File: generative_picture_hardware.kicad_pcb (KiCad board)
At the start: 2 copper layers, 100 x 100 mm, 73 parts, among them J1 e_Paper_HAT, J2 Conn_ARM_JTAG_SWD_10, J3 USB_C_Receptacle_USB2.0, Q1 PMN48XP, Q2 DMG9926UDM, Q3 MBT3904DW1, SW1 SW_Push, SW2 SW_Push, U1 AP2112K-3.3, U2 ESP32-WROOM-32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

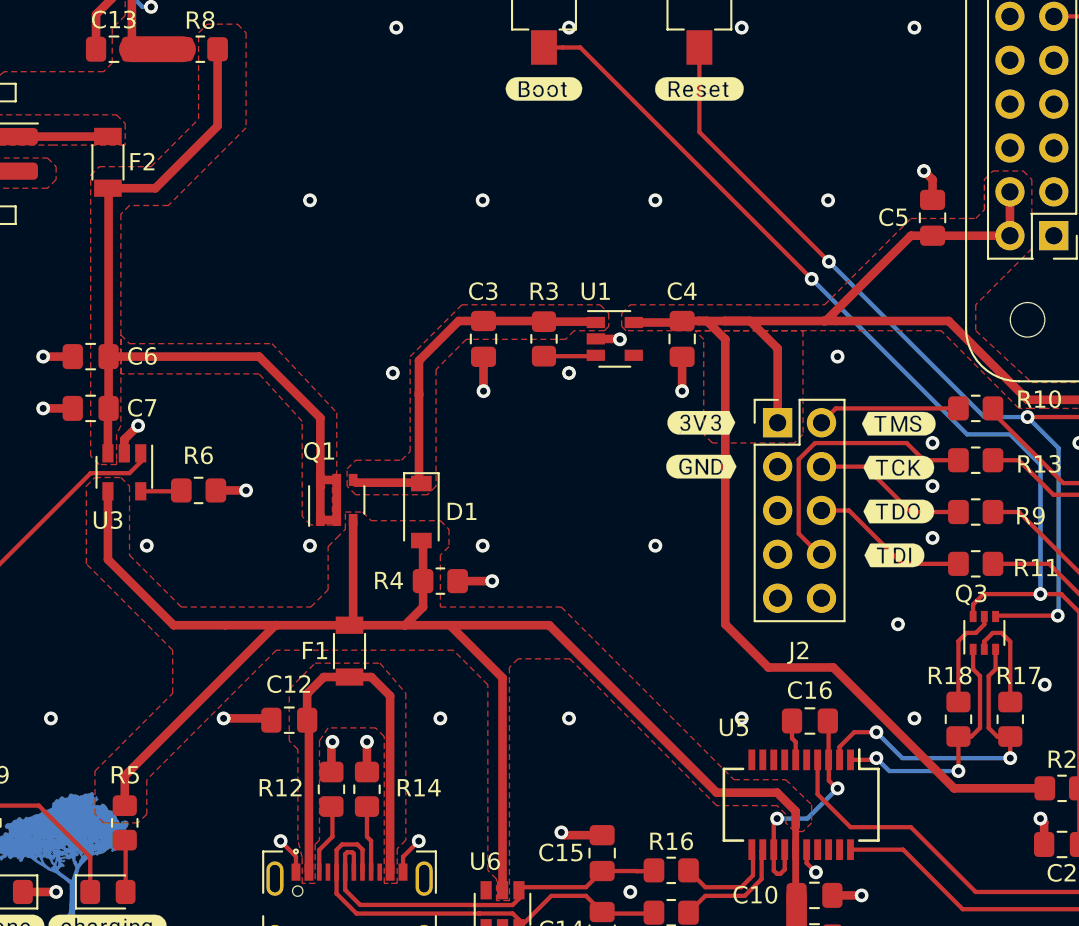
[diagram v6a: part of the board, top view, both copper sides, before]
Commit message: Adjusts some of the interactions between pads and copper fills
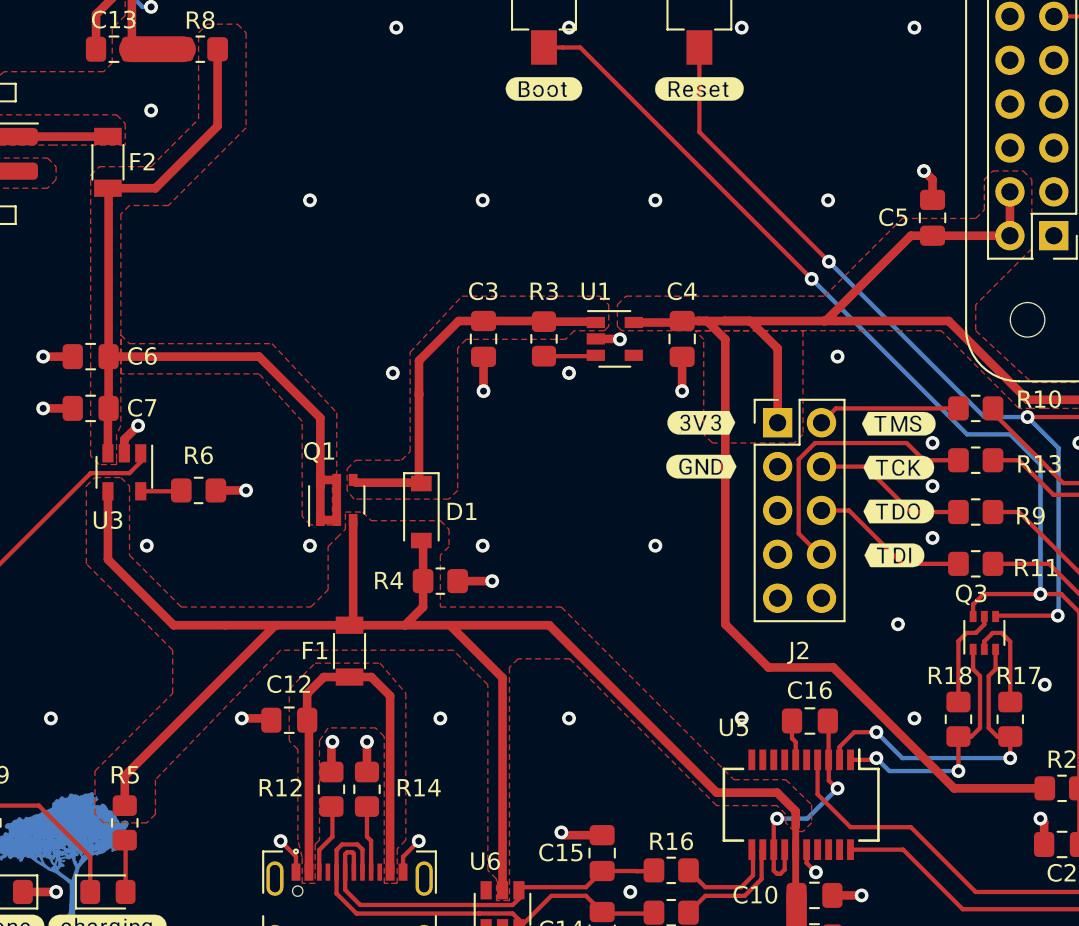
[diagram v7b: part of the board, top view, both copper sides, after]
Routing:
- net GND: track 85.4 -> 84.4 mm, vias 111 -> 112
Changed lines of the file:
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@@
     (property "Sheetfile" "generative_picture_hardware.kicad_sch")
     (property "Sheetname" "")
+    (zone_connect 2)
     (attr smd)
     (fp_text reference "U1" (at -1.1 -2.725) (layer "F.SilkS")
@@
     (fp_line (start 0.9 -1.55) (end 0.9 1.55) (layer "F.Fab") (width 0.1))
     (pad "1" smd rect (at -1.1 -0.95) (locked) (size 1.06 0.65) (layers "F.Cu" "F.Paste" "F.Mask")
-      (net 6 "VCC") (pinfunction "VIN"))
+      (net 6 "VCC") (pinfunction "VIN") (zone_connect 2))
     (pad "2" smd rect (at -1.1 0) (locked) (size 1.06 0.65) (layers "F.Cu" "F.Paste" "F.Mask")
-      (net 3 "GND") (pinfunction "GND"))
+      (net 3 "GND") (pinfunction "GND") (zone_connect 2))
     (pad "3" smd rect (at -1.1 0.95) (locked) (size 1.06 0.65) (layers "F.Cu" "F.Paste" "F.Mask")
-      (net 65 "Net-(R3-Pad2)") (pinfunction "EN"))
+      (net 65 "Net-(R3-Pad2)") (pinfunction "EN") (zone_connect 2))
     (pad "4" smd rect (at 1.1 0.95) (locked) (size 1.06 0.65) (layers "F.Cu" "F.Paste" "F.Mask")
-      (net 81 "unconnected-(U1-Pad4)") (pinfunction "NC"))
+      (net 81 "unconnected-(U1-Pad4)") (pinfunction "NC") (zone_connect 2))
     (pad "5" smd rect (at 1.1 -0.95) (locked) (size 1.06 0.65) (layers "F.Cu" "F.Paste" "F.Mask")
-      (net 7 "+3V3") (pinfunction "VOUT"))
+      (net 7 "+3V3") (pinfunction "VOUT") (zone_connect 2))
     (model "${KISYS3DMOD}/Package_TO_SOT_SMD.3dshapes/SOT-23-5.wrl"
       (offset (xyz 0 0 0))
@@
       (net 9 "+5V") (pinfunction "G"))
     (pad "4" smd rect (at 1.16 0.95 90) (locked) (size 0.7 0.51) (layers "F.Cu" "F.Paste" "F.Mask")
-      (net 6 "VCC") (pinfunction "S"))
+      (net 6 "VCC") (pinfunction "S") (zone_connect 2))
     (pad "5" smd rect (at 1.16 0 90) (locked) (size 0.7 0.51) (layers "F.Cu" "F.Paste" "F.Mask")
       (net 8 "+BATT") (pinfunction "D"))
@@
       (net 8 "+BATT") (pinfunction "VBAT"))
     (pad "4" smd rect (at 1.1 0.95 270) (locked) (size 1.06 0.65) (layers "F.Cu" "F.Paste" "F.Mask")
-      (net 9 "+5V") (pinfunction "VDD"))
+      (net 9 "+5V") (pinfunction "VDD") (zone_connect 2))
     (pad "5" smd rect (at 1.1 -0.95 270) (locked) (size 1.06 0.65) (layers "F.Cu" "F.Paste" "F.Mask")
       (net 66 "Net-(R6-Pad1)") (pinfunction "PROG"))
@@
   (segment (start 156.75 145.8625) (end 156.21 145.3225) (width 0.25) (layer "F.Cu") (net 3))
   (segment (start 141 88) (end 141 89.9) (width 0.5) (layer "F.Cu") (net 3))
-  (segment (start 122.449748 136.949748) (end 125.10815 136.949748) (width 0.5) (layer "F.Cu") (net 3))
   (segment (start 128.6925 140.054098) (end 128.6925 138.361598) (width 0.5) (layer "F.Cu") (net 3))
   (segment (start 131.14 150.051598) (end 131.948402 150.051598) (width 0.5) (layer "F.Cu") (net 3))
@@
   (segment (start 192.25 141.25) (end 192.255 141.255) (width 0.5) (layer "F.Cu") (net 3))
   (segment (start 174.745 129.245) (end 174.25 128.75) (width 0.5) (layer "F.Cu") (net 3))
+  (segment (start 123.5 136.949748) (end 125.10815 136.949748) (width 0.5) (layer "F.Cu") (net 3))
   (segment (start 184.755 131.505) (end 184.75 131.5) (width 0.5) (layer "F.Cu") (net 3))
   (segment (start 128.6925 138.361598) (end 128.75 138.304098) (width 0.5) (layer "F.Cu") (net 3))
@@
   (via (at 146 147) (size 0.8) (drill 0.4) (layers "F.Cu" "B.Cu") (free) (net 3))
   (via (at 102.449748 116.949748) (size 0.8) (drill 0.4) (layers "F.Cu" "B.Cu") (free) (net 3))
+  (via (at 123.5 136.949748) (size 0.8) (drill 0.4) (layers "F.Cu" "B.Cu") (free) (net 3))
   (via (at 142.00625 143.55) (size 0.8) (drill 0.4) (layers "F.Cu" "B.Cu") (net 3))
   (via (at 142.449748 116.949748) (size 0.8) (drill 0.4) (layers "F.Cu" "B.Cu") (free) (net 3))
   (via (at 197.449748 86.949748) (size 0.8) (drill 0.4) (layers "F.Cu" "B.Cu") (free) (net 3))
   (via (at 197.449748 66.949748) (size 0.8) (drill 0.4) (layers "F.Cu" "B.Cu") (free) (net 3))
-  (via (at 122.449748 136.949748) (size 0.8) (drill 0.4) (layers "F.Cu" "B.Cu") (free) (net 3))
   (via (at 107.449748 86.949748) (size 0.8) (drill 0.4) (layers "F.Cu" "B.Cu") (free) (net 3))
   (via (at 112 119) (size 0.8) (drill 0.4) (layers "F.Cu" "B.Cu") (net 3))
@@
   (via (at 147.449748 126.949748) (size 0.8) (drill 0.4) (layers "F.Cu" "B.Cu") (free) (net 3))
   (via (at 174.25 128.75) (size 0.8) (drill 0.4) (layers "F.Cu" "B.Cu") (net 3))
+  (via (at 118.25 101.75) (size 0.8) (drill 0.4) (layers "F.Cu" "B.Cu") (free) (net 3))
   (via (at 187.449748 66.949748) (size 0.8) (drill 0.4) (layers "F.Cu" "B.Cu") (free) (net 3))
   (via (at 192.25 141.25) (size 0.8) (drill 0.4) (layers "F.Cu" "B.Cu") (net 3))
@@
     (polygon
       (pts
-        (xy 144.75 113.5)
+        (xy 144.75 113)
         (xy 144.75 114.25)
         (xy 144.5 114.5)
@@
         (xy 142.25 115)
         (xy 136.5 115)
-        (xy 134.75 116.75)
-        (xy 134.75 123.5)
-        (xy 134.25 124)
-        (xy 130.1 124)
-        (xy 129.6 123.5)
+        (xy 136 115.5)
+        (xy 136 123.75)
+        (xy 135.5 124.25)
+        (xy 130 124.25)
+        (xy 129.6 123.75)
         (xy 129.6 122.5)
         (xy 130.1 122)
         (xy 132.75 122)
         (xy 133.25 121.5)
-        (xy 133.25 116)
-        (xy 136.25 113)
-        (xy 144.25 113)
+        (xy 133.25 115.75)
+        (xy 136.25 112.5)
+        (xy 144.25 112.5)
       )
     )
@@
         (xy 168.5 119)
         (xy 164 114.5)
-        (xy 145.75 114.5)
-        (xy 145.5 114.25)
-        (xy 145.5 113.5)
-        (xy 146 113)
-        (xy 157.25 113)
-        (xy 162.25 108)
+        (xy 145.5 114.5)
+        (xy 145.25 114.25)
+        (xy 145.25 113)
+        (xy 145.75 112.5)
+        (xy 157.25 112.5)
+        (xy 161.75 108)
         (xy 166 108)
         (xy 166.5 107.5)
@@
         (xy 137.75 135)
         (xy 135.75 133)
-        (xy 125.5 133)
-        (xy 118 140.5)
-        (xy 118 142.5)
-        (xy 117.5 143)
+        (xy 125.75 133)
+        (xy 118.5 140.5)
+        (xy 118.5 142.5)
+        (xy 118 143)
         (xy 115.5 143)
         (xy 115 142.5)

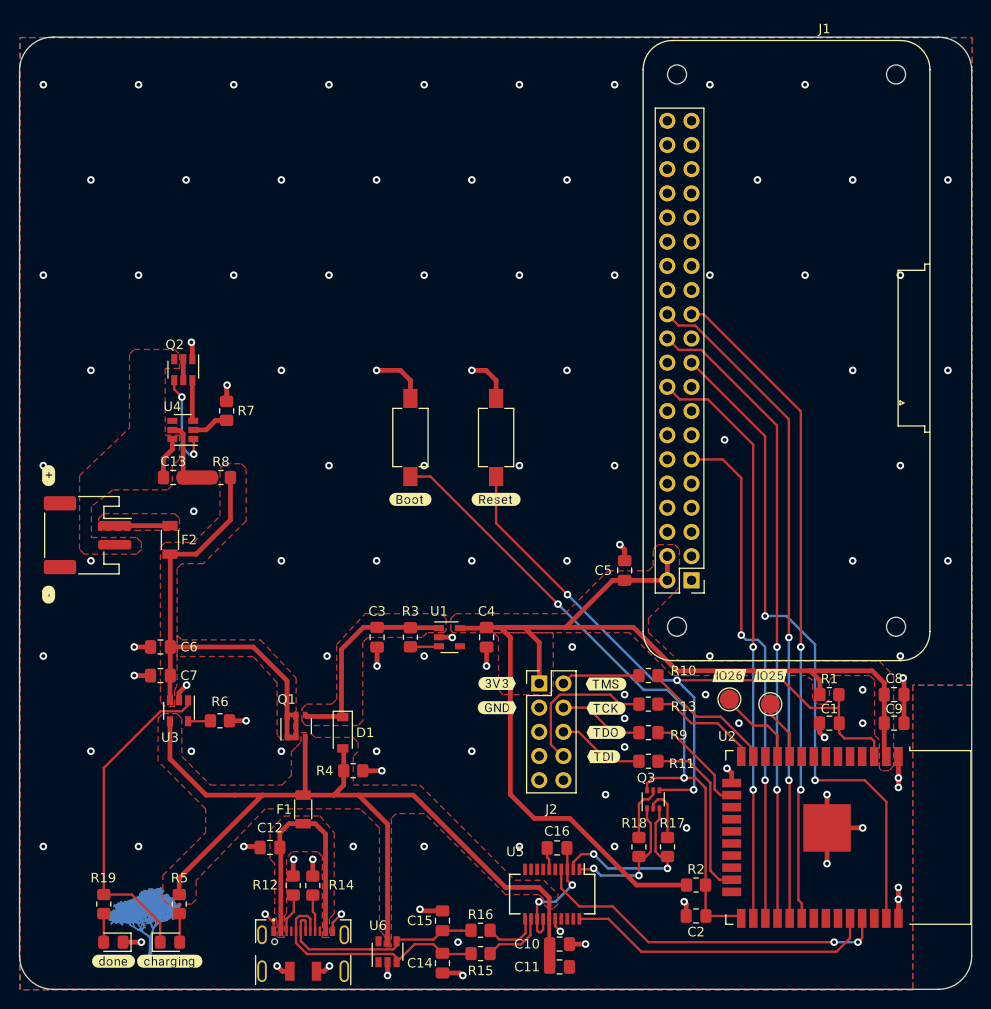
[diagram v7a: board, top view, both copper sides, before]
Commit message: Adds JLCPCB order number placeholder adjusts silkscreen some more
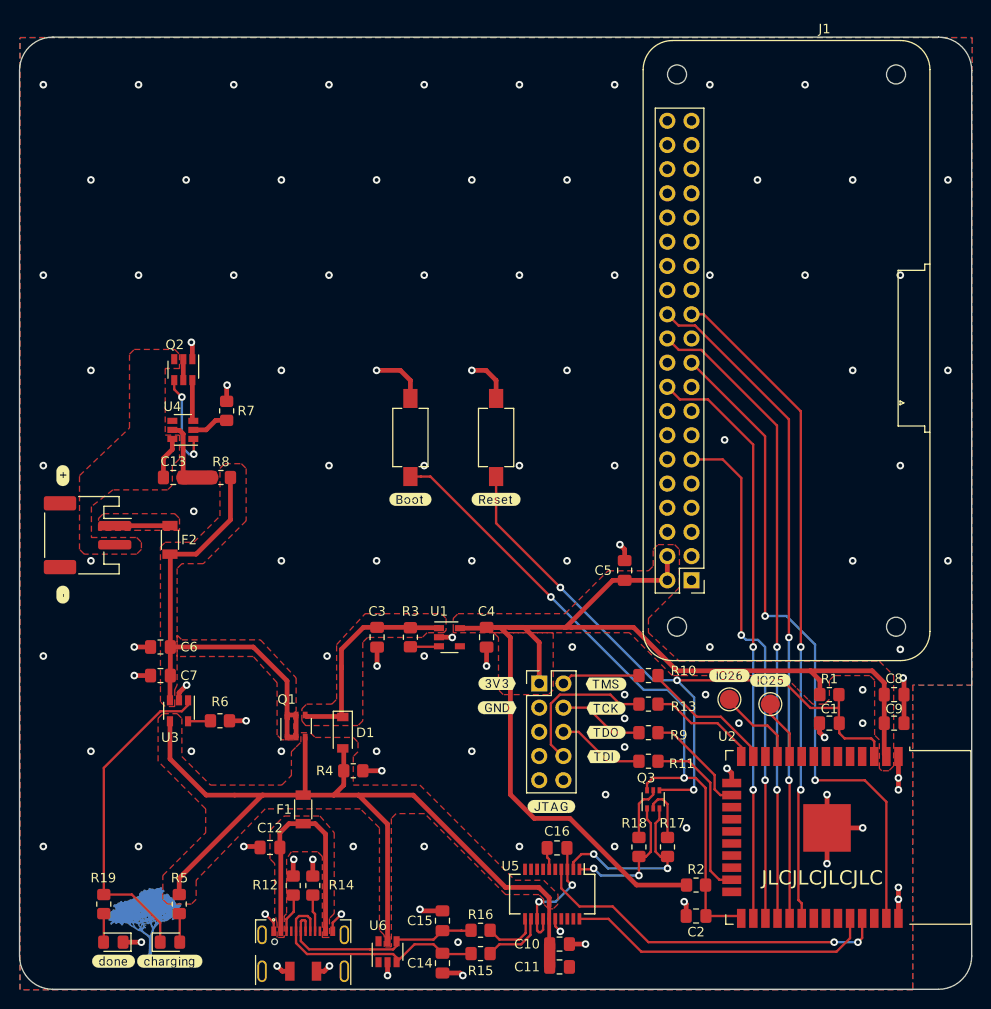
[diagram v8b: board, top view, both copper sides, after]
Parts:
- removed the ? at (178.8, 119.0)
- added ?: , buzzardLabel, F.Cu at (178.8, 119.5)
- added ?: , buzzardLabel, F.Cu at (155.8, 132.8)
- moved ? 1.50 mm to (104.5, 98.0)
- moved ? 1.50 mm to (104.5, 110.5)
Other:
- board text added: "JLCJLCJLCJLC"
